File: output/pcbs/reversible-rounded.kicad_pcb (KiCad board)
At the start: 2 copper layers, 159.5 x 127.3 mm, 72 parts

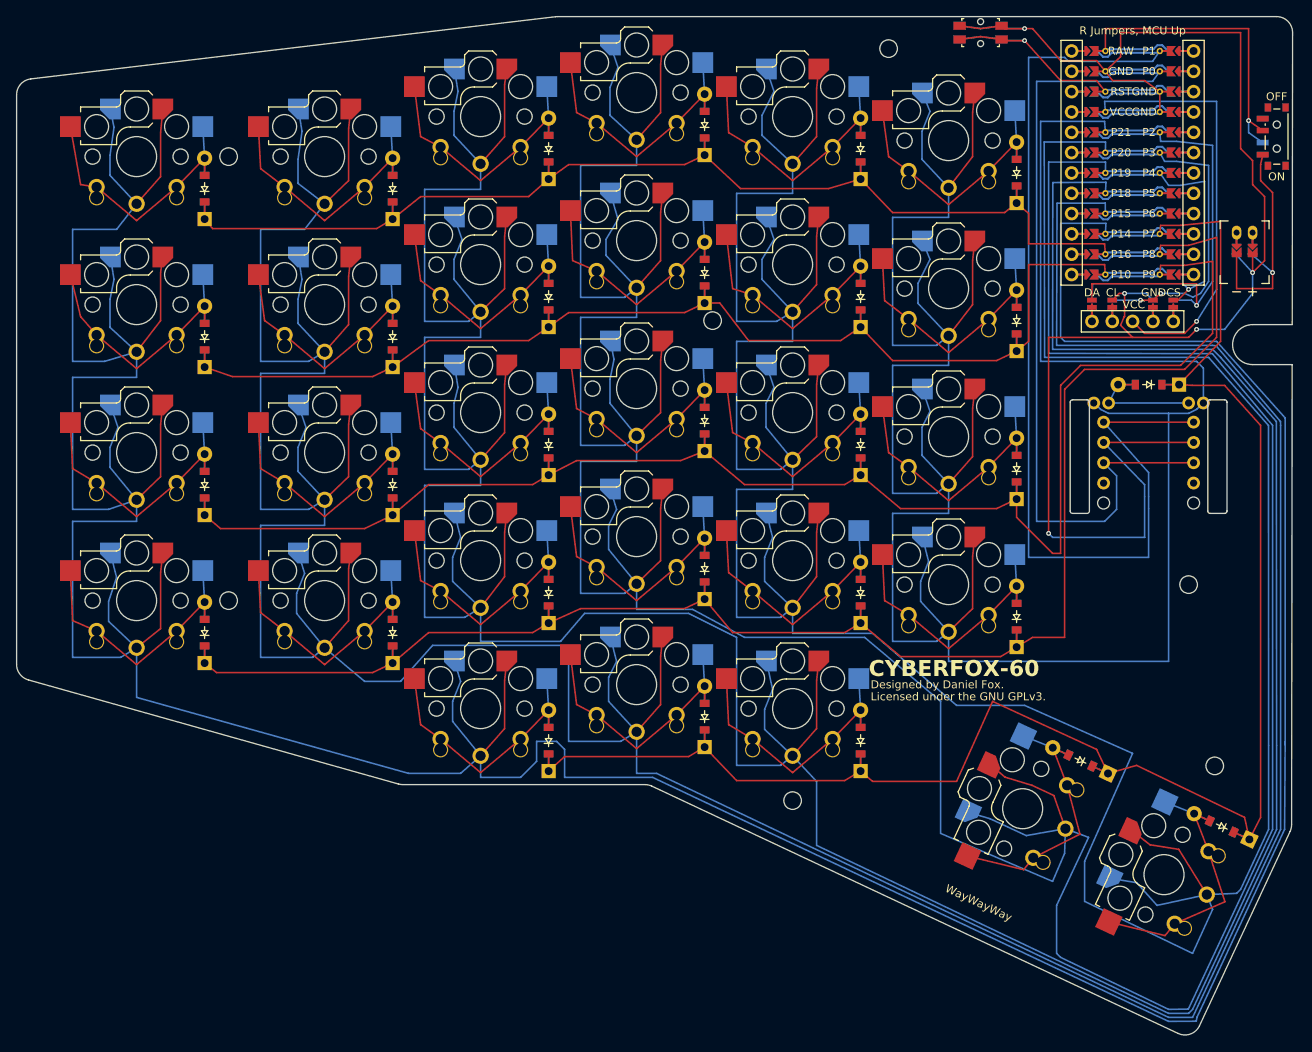
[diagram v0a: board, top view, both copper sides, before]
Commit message: The PCB's wiring is completed.  May need additional touchup.
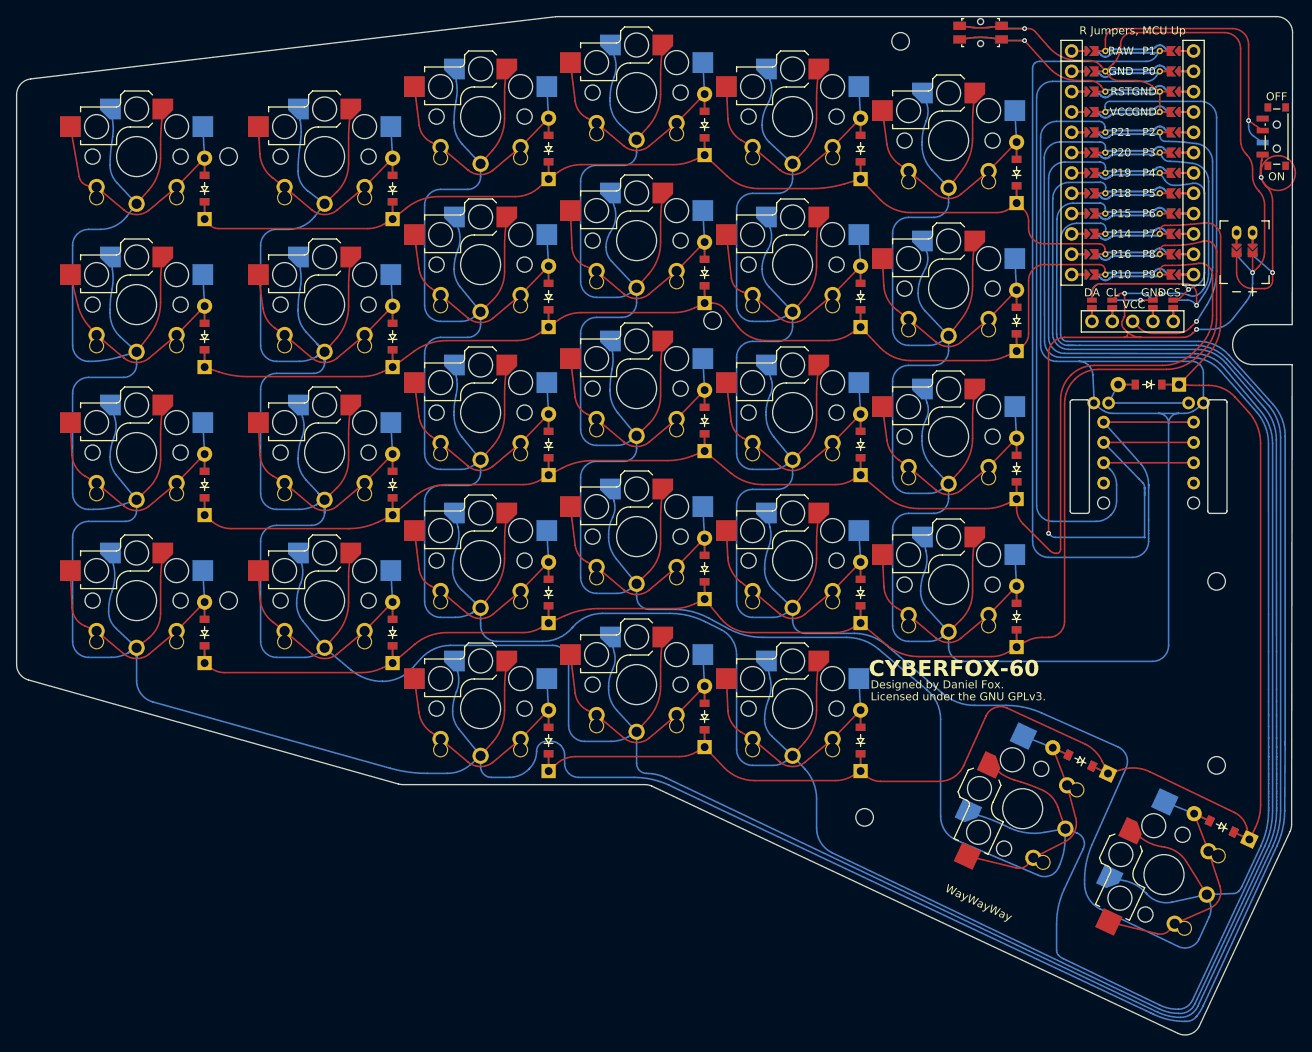
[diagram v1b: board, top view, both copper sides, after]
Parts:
- moved MH7 9.24 mm to (120.5, 117.0)
- moved MH2 3.52 mm to (164.5, 87.5)
- moved MH3 1.75 mm to (125.0, 20.0)
- moved MH1 0.24 mm to (164.5, 110.5)
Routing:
- net P19: track 504.9 -> 489.6 mm
- net P20: track 470.0 -> 456.2 mm
- net P14: track 538.0 -> 525.5 mm
- net P18: track 507.2 -> 496.7 mm
- net BAT_P: track 29.4 -> 39.2 mm, vias 1 -> 2
- net P8: track 224.2 -> 219.4 mm
- net P1: track 134.9 -> 130.5 mm
- net P15: track 519.8 -> 515.6 mm
- net P9: track 213.3 -> 209.5 mm
- net P21: track 359.7 -> 356.1 mm
- net GND: track 231.3 -> 227.8 mm
- net P0: track 109.2 -> 106.7 mm
- net P2: track 59.1 -> 56.6 mm
- net P7: track 236.1 -> 234.0 mm
- net P10: track 167.4 -> 165.3 mm
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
